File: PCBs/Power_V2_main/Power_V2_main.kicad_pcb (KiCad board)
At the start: 2 copper layers, 53 parts, among them IC2 ADS1115BQDGSRQ1, IC3 ADS1115BQDGSRQ1, J1 Conn_01x02, J11 Conn_01x04, J12 Conn_01x02, J13 Conn_01x04, J14 Conn_01x04, J18 YK4420203000G, J2 Conn_01x02, J3 Conn_01x02, J4 PCIE-164-02-F-D-TH-TR, J5 PCIE-164-02-F-D-TH-TR, J6 PCIE-164-02-F-D-TH-TR, J7 USB_C_Receptacle_USB2.0_16P, J8 PCIE-164-02-F-D-TH-TR, Q4 NTD25P03LT4G, U2 ESP32-S3, U3 USBLC6-2SC6, U4 178.6164.0001, U5 TVS3300DRV, U9 AMS1117-3.3

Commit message: finished secondary and beginning layout of main
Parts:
- moved J5 242.8 mm to (236.8, 224.2), turned to 180 degrees
- moved J1 232.2 mm to (280.0, 63.0)
- moved J3 232.2 mm to (292.3, 63.0)
- moved J2 216.7 mm to (265.5, 82.0), turned to -90 degrees
- moved J4 214.2 mm to (236.8, 199.2), turned to 180 degrees
- moved J12 198.0 mm to (265.0, 129.5), turned to 90 degrees
- moved J18 191.7 mm to (265.8, 104.8), turned to -90 degrees
- moved J6 188.7 mm to (236.8, 174.2), turned to 180 degrees
- moved J8 167.7 mm to (236.8, 149.2), turned to 180 degrees
- moved C12 116.3 mm to (9.14, 152.8)
- moved C14 116.3 mm to (-10.1, 194.6)
- moved C17 116.3 mm to (9.14, 160.4)
- moved D3 116.3 mm to (1.31, 174.0)
- moved IC3 116.3 mm to (22.8, 183.8)
- moved J7 116.3 mm to (17.2, 171.5)
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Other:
- board outline added: 100 x 200 mm

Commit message: shortened main board and secondary
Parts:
- removed the J7 at (17.2, 171.5)
- removed RESET1: PTS645SK43SMTR92LFS, IPRL_footprints:PTS645SK43SMTR92LFS
- removed S1: SK12F14G5, IPRL_footprints:SK12F14G5
- removed U4: 178.6164.0001, IPRL_footprints:178.6164.XXX1
- added J7: TYPE-C-31-M-12, iprl_footprints:TYPE-C-31-M-12, F.Cu at (142.9, 216.3)
- added J7: USB_C_Receptacle_USB2.0_16P, iprl_footprints:USB_C_16P, F.Cu at (131.9, 180.4)
- added R20: 5.1k, Resistor_SMD:R_0805_2012Metric, F.Cu at (139.1, 221.1)
- added R21: 5.1k, Resistor_SMD:R_0805_2012Metric, F.Cu at (139.1, 224.1)
- added U6: USBLC6-4SC6, Package_TO_SOT_SMD:SOT-23-6, F.Cu at (143.9, 222.1)
- BOOT1: footprint IPRL_footprints:PTS645SK43SMTR92LFS -> iprl_footprints:PTS645SK43SMTR92LFS
- D1: footprint IPRL_footprints:SODFL1608X70N -> iprl_footprints:SODFL1608X70N
- D4: footprint IPRL_footprints:DIOM8059X265N -> iprl_footprints:DIOM8059X265N
- IC2, IC3: footprint IPRL_footprints:SOP50P490X110-10N -> iprl_footprints:SOP50P490X110-10N
- J18: footprint IPRL_footprints:RHDR2W120P0X950_1X2_2050X1430X1790P -> iprl_footprints:RHDR2W120P0X950_1X2_2050X1430X1790P
- J4, J5, J6, J8: footprint IPRL_footprints:SAMTEC_PCIE-164-02-F-D-TH-TR -> iprl_footprints:SAMTEC_PCIE-164-02-F-D-TH-TR
- Q4: footprint IPRL_footprints:MJD45H11T4G -> iprl_footprints:MJD45H11T4G
- moved C14 180.9 mm to (159.9, 132.8)
- moved C9 180.9 mm to (159.9, 129.8)
- moved D4 175.6 mm to (154.4, 158.7)
- moved J1 174.3 mm to (119.9, 132.0)
- moved J3 174.3 mm to (132.1, 132.0)
- moved IC2 166.4 mm to (180.9, 127.3)
- moved IC3 166.4 mm to (180.9, 132.0)
- moved R1 166.4 mm to (179.4, 135.8)
- moved R3 166.4 mm to (179.4, 138.7)
- moved R5 166.4 mm to (179.4, 141.7)
- moved D7 165.1 mm to (156.5, 126.7)
- moved U5 161.7 mm to (159.8, 136.2)
- moved R4 159.8 mm to (161.1, 164.1)
- moved R7 159.8 mm to (161.1, 167.1)
- moved R8 159.8 mm to (161.1, 170.0)
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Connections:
- D7 pad 1: /Protection and power/14V8_PROTECTED -> /14V8_PROTECTED
- J4 pad A12: /Connector Arm/14V8_OUT -> /14V8_PROTECTED
- J4 pad A13: /Connector Arm/14V8_OUT -> /14V8_PROTECTED
- J4 pad A14: /Connector Arm/14V8_OUT -> /14V8_PROTECTED
- J4 pad A15: /Connector Arm/14V8_OUT -> /14V8_PROTECTED
- J4 pad A16: /Connector Arm/14V8_OUT -> /14V8_PROTECTED
- J4 pad A17: /Connector Arm/14V8_OUT -> /14V8_PROTECTED
- J4 pad A18: /Connector Arm/14V8_OUT -> /14V8_PROTECTED
- J4 pad A19: /Connector Arm/14V8_OUT -> /14V8_PROTECTED
- J4 pad A20: /Connector Arm/14V8_OUT -> /14V8_PROTECTED
- J4 pad A21: /Connector Arm/14V8_OUT -> /14V8_PROTECTED
- J4 pad A22: /Connector Arm/14V8_OUT -> /14V8_PROTECTED
- J4 pad A23: /Connector Arm/14V8_OUT -> /14V8_PROTECTED
- J4 pad A24: /Connector Arm/14V8_OUT -> /14V8_PROTECTED
- J4 pad A25: /Connector Arm/14V8_OUT -> /14V8_PROTECTED
- J4 pad A26: /Connector Arm/14V8_OUT -> /14V8_PROTECTED
- J4 pad A27: /Connector Arm/14V8_OUT -> /14V8_PROTECTED
- J4 pad A28: /Connector Arm/14V8_OUT -> /14V8_PROTECTED
- J4 pad A29: /Connector Arm/14V8_OUT -> /14V8_PROTECTED
- J4 pad A30: /Connector Arm/14V8_OUT -> /14V8_PROTECTED
- J4 pad A31: /Connector Arm/14V8_OUT -> /14V8_PROTECTED
- J4 pad A32: /Connector Arm/14V8_OUT -> /14V8_PROTECTED
- J4 pad A33: /Connector Arm/14V8_OUT -> /14V8_PROTECTED
- J4 pad A34: /Connector Arm/14V8_OUT -> /14V8_PROTECTED
- J4 pad A35: /Connector Arm/14V8_OUT -> /14V8_PROTECTED
- J4 pad A36: /Connector Arm/14V8_OUT -> /14V8_PROTECTED
- J4 pad A37: /Connector Arm/14V8_OUT -> /14V8_PROTECTED
- J4 pad A38: /Connector Arm/14V8_OUT -> /14V8_PROTECTED
- J4 pad A39: /Connector Arm/14V8_OUT -> /14V8_PROTECTED
- J4 pad A40: /Connector Arm/14V8_OUT -> /14V8_PROTECTED
- J4 pad A41: /Connector Arm/14V8_OUT -> /14V8_PROTECTED
- J4 pad A42: /Connector Arm/14V8_OUT -> /14V8_PROTECTED
- J4 pad A43: /Connector Arm/14V8_OUT -> /14V8_PROTECTED
- J4 pad A44: /Connector Arm/14V8_OUT -> /14V8_PROTECTED
- J4 pad A45: /Connector Arm/14V8_OUT -> /14V8_PROTECTED
- J4 pad A46: /Connector Arm/14V8_OUT -> /14V8_PROTECTED
- J4 pad A47: /Connector Arm/14V8_OUT -> /14V8_PROTECTED
- J4 pad A48: /Connector Arm/14V8_OUT -> /14V8_PROTECTED
- J4 pad A49: /Connector Arm/14V8_OUT -> /14V8_PROTECTED
- J4 pad A50: /Connector Arm/14V8_OUT -> /14V8_PROTECTED
- J4 pad A51: /Connector Arm/14V8_OUT -> /14V8_PROTECTED
- J4 pad A52: /Connector Arm/14V8_OUT -> /14V8_PROTECTED
- J4 pad A53: /Connector Arm/14V8_OUT -> /14V8_PROTECTED
- J4 pad A54: /Connector Arm/14V8_OUT -> /14V8_PROTECTED
- J4 pad A55: /Connector Arm/14V8_OUT -> /14V8_PROTECTED
- J4 pad A56: /Connector Arm/14V8_OUT -> /14V8_PROTECTED
- J4 pad A57: /Connector Arm/14V8_OUT -> /14V8_PROTECTED
- J4 pad A58: /Connector Arm/14V8_OUT -> /14V8_PROTECTED
- J4 pad A59: /Connector Arm/14V8_OUT -> /14V8_PROTECTED
- J4 pad A60: /Connector Arm/14V8_OUT -> /14V8_PROTECTED
- J4 pad A61: /Connector Arm/14V8_OUT -> /14V8_PROTECTED
- J4 pad A62: /Connector Arm/14V8_OUT -> /14V8_PROTECTED
- J4 pad A63: /Connector Arm/14V8_OUT -> /14V8_PROTECTED
- J4 pad A64: /Connector Arm/14V8_OUT -> /14V8_PROTECTED
- J4 pad A65: /Connector Arm/14V8_OUT -> /14V8_PROTECTED
- J4 pad A66: /Connector Arm/14V8_OUT -> /14V8_PROTECTED
- J4 pad A67: /Connector Arm/14V8_OUT -> /14V8_PROTECTED
- J4 pad A68: /Connector Arm/14V8_OUT -> /14V8_PROTECTED
- J4 pad A69: /Connector Arm/14V8_OUT -> /14V8_PROTECTED
- J4 pad A70: /Connector Arm/14V8_OUT -> /14V8_PROTECTED
- J4 pad A71: /Connector Arm/14V8_OUT -> /14V8_PROTECTED
- J4 pad A72: /Connector Arm/14V8_OUT -> /14V8_PROTECTED
- J4 pad A73: /Connector Arm/14V8_OUT -> /14V8_PROTECTED
- J4 pad A74: /Connector Arm/14V8_OUT -> /14V8_PROTECTED
- J4 pad A75: /Connector Arm/14V8_OUT -> /14V8_PROTECTED
- J4 pad A76: /Connector Arm/14V8_OUT -> /14V8_PROTECTED
- J4 pad A77: /Connector Arm/14V8_OUT -> /14V8_PROTECTED
- J4 pad A78: /Connector Arm/14V8_OUT -> /14V8_PROTECTED
- J4 pad A79: /Connector Arm/14V8_OUT -> /14V8_PROTECTED
- J4 pad A80: /Connector Arm/14V8_OUT -> /14V8_PROTECTED
- J4 pad A81: /Connector Arm/14V8_OUT -> /14V8_PROTECTED
- J4 pad A82: /Connector Arm/14V8_OUT -> /14V8_PROTECTED
- J5 pad A12: /Connector Comms/14V8_OUT -> /14V8_PROTECTED
- J5 pad A13: /Connector Comms/14V8_OUT -> /14V8_PROTECTED
- J5 pad A14: /Connector Comms/14V8_OUT -> /14V8_PROTECTED
- J5 pad A15: /Connector Comms/14V8_OUT -> /14V8_PROTECTED
- J5 pad A16: /Connector Comms/14V8_OUT -> /14V8_PROTECTED
- J5 pad A17: /Connector Comms/14V8_OUT -> /14V8_PROTECTED
- J5 pad A18: /Connector Comms/14V8_OUT -> /14V8_PROTECTED
- J5 pad A19: /Connector Comms/14V8_OUT -> /14V8_PROTECTED
- J5 pad A20: /Connector Comms/14V8_OUT -> /14V8_PROTECTED
- J5 pad A21: /Connector Comms/14V8_OUT -> /14V8_PROTECTED
- J5 pad A22: /Connector Comms/14V8_OUT -> /14V8_PROTECTED
- J5 pad A23: /Connector Comms/14V8_OUT -> /14V8_PROTECTED
- J5 pad A24: /Connector Comms/14V8_OUT -> /14V8_PROTECTED
- J5 pad A25: /Connector Comms/14V8_OUT -> /14V8_PROTECTED
- J5 pad A26: /Connector Comms/14V8_OUT -> /14V8_PROTECTED
- J5 pad A27: /Connector Comms/14V8_OUT -> /14V8_PROTECTED
- J5 pad A28: /Connector Comms/14V8_OUT -> /14V8_PROTECTED
- J5 pad A29: /Connector Comms/14V8_OUT -> /14V8_PROTECTED
- J5 pad A30: /Connector Comms/14V8_OUT -> /14V8_PROTECTED
- J5 pad A31: /Connector Comms/14V8_OUT -> /14V8_PROTECTED
- J5 pad A32: /Connector Comms/14V8_OUT -> /14V8_PROTECTED
- J5 pad A33: /Connector Comms/14V8_OUT -> /14V8_PROTECTED
- J5 pad A34: /Connector Comms/14V8_OUT -> /14V8_PROTECTED
- J5 pad A35: /Connector Comms/14V8_OUT -> /14V8_PROTECTED
- J5 pad A36: /Connector Comms/14V8_OUT -> /14V8_PROTECTED
- J5 pad A37: /Connector Comms/14V8_OUT -> /14V8_PROTECTED
- J5 pad A38: /Connector Comms/14V8_OUT -> /14V8_PROTECTED
- J5 pad A39: /Connector Comms/14V8_OUT -> /14V8_PROTECTED
- J5 pad A40: /Connector Comms/14V8_OUT -> /14V8_PROTECTED
- J5 pad A41: /Connector Comms/14V8_OUT -> /14V8_PROTECTED
- J5 pad A42: /Connector Comms/14V8_OUT -> /14V8_PROTECTED
- J5 pad A43: /Connector Comms/14V8_OUT -> /14V8_PROTECTED
- J5 pad A44: /Connector Comms/14V8_OUT -> /14V8_PROTECTED
- J5 pad A45: /Connector Comms/14V8_OUT -> /14V8_PROTECTED
- J5 pad A46: /Connector Comms/14V8_OUT -> /14V8_PROTECTED
- J5 pad A47: /Connector Comms/14V8_OUT -> /14V8_PROTECTED
- J5 pad A48: /Connector Comms/14V8_OUT -> /14V8_PROTECTED
- J5 pad A49: /Connector Comms/14V8_OUT -> /14V8_PROTECTED
- J5 pad A50: /Connector Comms/14V8_OUT -> /14V8_PROTECTED
- J5 pad A51: /Connector Comms/14V8_OUT -> /14V8_PROTECTED
- J5 pad A52: /Connector Comms/14V8_OUT -> /14V8_PROTECTED
- J5 pad A53: /Connector Comms/14V8_OUT -> /14V8_PROTECTED
- J5 pad A54: /Connector Comms/14V8_OUT -> /14V8_PROTECTED
- J5 pad A55: /Connector Comms/14V8_OUT -> /14V8_PROTECTED
- J5 pad A56: /Connector Comms/14V8_OUT -> /14V8_PROTECTED
- J5 pad A57: /Connector Comms/14V8_OUT -> /14V8_PROTECTED
- J5 pad A58: /Connector Comms/14V8_OUT -> /14V8_PROTECTED
- J5 pad A59: /Connector Comms/14V8_OUT -> /14V8_PROTECTED
- J5 pad A60: /Connector Comms/14V8_OUT -> /14V8_PROTECTED
- J5 pad A61: /Connector Comms/14V8_OUT -> /14V8_PROTECTED
- J5 pad A62: /Connector Comms/14V8_OUT -> /14V8_PROTECTED
- J5 pad A63: /Connector Comms/14V8_OUT -> /14V8_PROTECTED
- J5 pad A64: /Connector Comms/14V8_OUT -> /14V8_PROTECTED
- J5 pad A65: /Connector Comms/14V8_OUT -> /14V8_PROTECTED
- J5 pad A66: /Connector Comms/14V8_OUT -> /14V8_PROTECTED
- J5 pad A67: /Connector Comms/14V8_OUT -> /14V8_PROTECTED
- J5 pad A68: /Connector Comms/14V8_OUT -> /14V8_PROTECTED
- J5 pad A69: /Connector Comms/14V8_OUT -> /14V8_PROTECTED
- J5 pad A70: /Connector Comms/14V8_OUT -> /14V8_PROTECTED
- J5 pad A71: /Connector Comms/14V8_OUT -> /14V8_PROTECTED
- J5 pad A72: /Connector Comms/14V8_OUT -> /14V8_PROTECTED
- J5 pad A73: /Connector Comms/14V8_OUT -> /14V8_PROTECTED
- J5 pad A74: /Connector Comms/14V8_OUT -> /14V8_PROTECTED
- J5 pad A75: /Connector Comms/14V8_OUT -> /14V8_PROTECTED
- J5 pad A76: /Connector Comms/14V8_OUT -> /14V8_PROTECTED
- J5 pad A77: /Connector Comms/14V8_OUT -> /14V8_PROTECTED
- J5 pad A78: /Connector Comms/14V8_OUT -> /14V8_PROTECTED
- J5 pad A79: /Connector Comms/14V8_OUT -> /14V8_PROTECTED
- J5 pad A80: /Connector Comms/14V8_OUT -> /14V8_PROTECTED
- J5 pad A81: /Connector Comms/14V8_OUT -> /14V8_PROTECTED
- J5 pad A82: /Connector Comms/14V8_OUT -> /14V8_PROTECTED
- J6 pad A12: /Connector Drive/14V8_OUT -> /14V8_PROTECTED
- J6 pad A13: /Connector Drive/14V8_OUT -> /14V8_PROTECTED
- J6 pad A14: /Connector Drive/14V8_OUT -> /14V8_PROTECTED
- J6 pad A15: /Connector Drive/14V8_OUT -> /14V8_PROTECTED
- J6 pad A16: /Connector Drive/14V8_OUT -> /14V8_PROTECTED
- J6 pad A17: /Connector Drive/14V8_OUT -> /14V8_PROTECTED
- J6 pad A18: /Connector Drive/14V8_OUT -> /14V8_PROTECTED
- J6 pad A19: /Connector Drive/14V8_OUT -> /14V8_PROTECTED
- J6 pad A20: /Connector Drive/14V8_OUT -> /14V8_PROTECTED
- J6 pad A21: /Connector Drive/14V8_OUT -> /14V8_PROTECTED
- J6 pad A22: /Connector Drive/14V8_OUT -> /14V8_PROTECTED
- J6 pad A23: /Connector Drive/14V8_OUT -> /14V8_PROTECTED
- J6 pad A24: /Connector Drive/14V8_OUT -> /14V8_PROTECTED
- J6 pad A25: /Connector Drive/14V8_OUT -> /14V8_PROTECTED
- J6 pad A26: /Connector Drive/14V8_OUT -> /14V8_PROTECTED
- J6 pad A27: /Connector Drive/14V8_OUT -> /14V8_PROTECTED
- J6 pad A28: /Connector Drive/14V8_OUT -> /14V8_PROTECTED
- J6 pad A29: /Connector Drive/14V8_OUT -> /14V8_PROTECTED
- J6 pad A30: /Connector Drive/14V8_OUT -> /14V8_PROTECTED
- J6 pad A31: /Connector Drive/14V8_OUT -> /14V8_PROTECTED
- J6 pad A32: /Connector Drive/14V8_OUT -> /14V8_PROTECTED
- J6 pad A33: /Connector Drive/14V8_OUT -> /14V8_PROTECTED
- J6 pad A34: /Connector Drive/14V8_OUT -> /14V8_PROTECTED
- J6 pad A35: /Connector Drive/14V8_OUT -> /14V8_PROTECTED
- J6 pad A36: /Connector Drive/14V8_OUT -> /14V8_PROTECTED
- J6 pad A37: /Connector Drive/14V8_OUT -> /14V8_PROTECTED
- J6 pad A38: /Connector Drive/14V8_OUT -> /14V8_PROTECTED
- J6 pad A39: /Connector Drive/14V8_OUT -> /14V8_PROTECTED
- J6 pad A40: /Connector Drive/14V8_OUT -> /14V8_PROTECTED
- J6 pad A41: /Connector Drive/14V8_OUT -> /14V8_PROTECTED
- J6 pad A42: /Connector Drive/14V8_OUT -> /14V8_PROTECTED
- J6 pad A43: /Connector Drive/14V8_OUT -> /14V8_PROTECTED
- J6 pad A44: /Connector Drive/14V8_OUT -> /14V8_PROTECTED
- J6 pad A45: /Connector Drive/14V8_OUT -> /14V8_PROTECTED
- J6 pad A46: /Connector Drive/14V8_OUT -> /14V8_PROTECTED
- J6 pad A47: /Connector Drive/14V8_OUT -> /14V8_PROTECTED
- J6 pad A48: /Connector Drive/14V8_OUT -> /14V8_PROTECTED
- J6 pad A49: /Connector Drive/14V8_OUT -> /14V8_PROTECTED
- J6 pad A50: /Connector Drive/14V8_OUT -> /14V8_PROTECTED
- J6 pad A51: /Connector Drive/14V8_OUT -> /14V8_PROTECTED
- J6 pad A52: /Connector Drive/14V8_OUT -> /14V8_PROTECTED
- J6 pad A53: /Connector Drive/14V8_OUT -> /14V8_PROTECTED
- J6 pad A54: /Connector Drive/14V8_OUT -> /14V8_PROTECTED
- J6 pad A55: /Connector Drive/14V8_OUT -> /14V8_PROTECTED
- J6 pad A56: /Connector Drive/14V8_OUT -> /14V8_PROTECTED
- J6 pad A57: /Connector Drive/14V8_OUT -> /14V8_PROTECTED
- J6 pad A58: /Connector Drive/14V8_OUT -> /14V8_PROTECTED
- J6 pad A59: /Connector Drive/14V8_OUT -> /14V8_PROTECTED
- J6 pad A60: /Connector Drive/14V8_OUT -> /14V8_PROTECTED
- J6 pad A61: /Connector Drive/14V8_OUT -> /14V8_PROTECTED
- J6 pad A62: /Connector Drive/14V8_OUT -> /14V8_PROTECTED
- J6 pad A63: /Connector Drive/14V8_OUT -> /14V8_PROTECTED
- J6 pad A64: /Connector Drive/14V8_OUT -> /14V8_PROTECTED
- J6 pad A65: /Connector Drive/14V8_OUT -> /14V8_PROTECTED
- J6 pad A66: /Connector Drive/14V8_OUT -> /14V8_PROTECTED
- J6 pad A67: /Connector Drive/14V8_OUT -> /14V8_PROTECTED
- J6 pad A68: /Connector Drive/14V8_OUT -> /14V8_PROTECTED
- J6 pad A69: /Connector Drive/14V8_OUT -> /14V8_PROTECTED
- J6 pad A70: /Connector Drive/14V8_OUT -> /14V8_PROTECTED
- J6 pad A71: /Connector Drive/14V8_OUT -> /14V8_PROTECTED
- J6 pad A72: /Connector Drive/14V8_OUT -> /14V8_PROTECTED
- J6 pad A73: /Connector Drive/14V8_OUT -> /14V8_PROTECTED
- J6 pad A74: /Connector Drive/14V8_OUT -> /14V8_PROTECTED
- J6 pad A75: /Connector Drive/14V8_OUT -> /14V8_PROTECTED
- J6 pad A76: /Connector Drive/14V8_OUT -> /14V8_PROTECTED
- J6 pad A77: /Connector Drive/14V8_OUT -> /14V8_PROTECTED
- J6 pad A78: /Connector Drive/14V8_OUT -> /14V8_PROTECTED
- J6 pad A79: /Connector Drive/14V8_OUT -> /14V8_PROTECTED
- J6 pad A80: /Connector Drive/14V8_OUT -> /14V8_PROTECTED
- J6 pad A81: /Connector Drive/14V8_OUT -> /14V8_PROTECTED
- J6 pad A82: /Connector Drive/14V8_OUT -> /14V8_PROTECTED
- J8 pad A12: /Connector Drill/14V8_OUT -> /14V8_PROTECTED
- J8 pad A13: /Connector Drill/14V8_OUT -> /14V8_PROTECTED
- J8 pad A14: /Connector Drill/14V8_OUT -> /14V8_PROTECTED
- J8 pad A15: /Connector Drill/14V8_OUT -> /14V8_PROTECTED
- J8 pad A16: /Connector Drill/14V8_OUT -> /14V8_PROTECTED
- J8 pad A17: /Connector Drill/14V8_OUT -> /14V8_PROTECTED
- J8 pad A18: /Connector Drill/14V8_OUT -> /14V8_PROTECTED
- J8 pad A19: /Connector Drill/14V8_OUT -> /14V8_PROTECTED
- J8 pad A20: /Connector Drill/14V8_OUT -> /14V8_PROTECTED
- J8 pad A21: /Connector Drill/14V8_OUT -> /14V8_PROTECTED
- J8 pad A22: /Connector Drill/14V8_OUT -> /14V8_PROTECTED
- J8 pad A23: /Connector Drill/14V8_OUT -> /14V8_PROTECTED
- J8 pad A24: /Connector Drill/14V8_OUT -> /14V8_PROTECTED
- J8 pad A25: /Connector Drill/14V8_OUT -> /14V8_PROTECTED
- J8 pad A26: /Connector Drill/14V8_OUT -> /14V8_PROTECTED
- J8 pad A27: /Connector Drill/14V8_OUT -> /14V8_PROTECTED
- J8 pad A28: /Connector Drill/14V8_OUT -> /14V8_PROTECTED
- J8 pad A29: /Connector Drill/14V8_OUT -> /14V8_PROTECTED
- J8 pad A30: /Connector Drill/14V8_OUT -> /14V8_PROTECTED
- J8 pad A31: /Connector Drill/14V8_OUT -> /14V8_PROTECTED
- J8 pad A32: /Connector Drill/14V8_OUT -> /14V8_PROTECTED
- J8 pad A33: /Connector Drill/14V8_OUT -> /14V8_PROTECTED
- J8 pad A34: /Connector Drill/14V8_OUT -> /14V8_PROTECTED
- J8 pad A35: /Connector Drill/14V8_OUT -> /14V8_PROTECTED
- J8 pad A36: /Connector Drill/14V8_OUT -> /14V8_PROTECTED
- J8 pad A37: /Connector Drill/14V8_OUT -> /14V8_PROTECTED
- J8 pad A38: /Connector Drill/14V8_OUT -> /14V8_PROTECTED
- J8 pad A39: /Connector Drill/14V8_OUT -> /14V8_PROTECTED
- J8 pad A40: /Connector Drill/14V8_OUT -> /14V8_PROTECTED
- J8 pad A41: /Connector Drill/14V8_OUT -> /14V8_PROTECTED
- J8 pad A42: /Connector Drill/14V8_OUT -> /14V8_PROTECTED
- J8 pad A43: /Connector Drill/14V8_OUT -> /14V8_PROTECTED
- J8 pad A44: /Connector Drill/14V8_OUT -> /14V8_PROTECTED
- J8 pad A45: /Connector Drill/14V8_OUT -> /14V8_PROTECTED
- J8 pad A46: /Connector Drill/14V8_OUT -> /14V8_PROTECTED
- J8 pad A47: /Connector Drill/14V8_OUT -> /14V8_PROTECTED
- J8 pad A48: /Connector Drill/14V8_OUT -> /14V8_PROTECTED
- J8 pad A49: /Connector Drill/14V8_OUT -> /14V8_PROTECTED
- J8 pad A50: /Connector Drill/14V8_OUT -> /14V8_PROTECTED
- J8 pad A51: /Connector Drill/14V8_OUT -> /14V8_PROTECTED
- J8 pad A52: /Connector Drill/14V8_OUT -> /14V8_PROTECTED
- J8 pad A53: /Connector Drill/14V8_OUT -> /14V8_PROTECTED
- J8 pad A54: /Connector Drill/14V8_OUT -> /14V8_PROTECTED
- J8 pad A55: /Connector Drill/14V8_OUT -> /14V8_PROTECTED
- J8 pad A56: /Connector Drill/14V8_OUT -> /14V8_PROTECTED
- J8 pad A57: /Connector Drill/14V8_OUT -> /14V8_PROTECTED
- J8 pad A58: /Connector Drill/14V8_OUT -> /14V8_PROTECTED
- J8 pad A59: /Connector Drill/14V8_OUT -> /14V8_PROTECTED
- J8 pad A60: /Connector Drill/14V8_OUT -> /14V8_PROTECTED
- J8 pad A61: /Connector Drill/14V8_OUT -> /14V8_PROTECTED
- J8 pad A62: /Connector Drill/14V8_OUT -> /14V8_PROTECTED
- J8 pad A63: /Connector Drill/14V8_OUT -> /14V8_PROTECTED
- J8 pad A64: /Connector Drill/14V8_OUT -> /14V8_PROTECTED
- J8 pad A65: /Connector Drill/14V8_OUT -> /14V8_PROTECTED
- J8 pad A66: /Connector Drill/14V8_OUT -> /14V8_PROTECTED
- J8 pad A67: /Connector Drill/14V8_OUT -> /14V8_PROTECTED
- J8 pad A68: /Connector Drill/14V8_OUT -> /14V8_PROTECTED
- J8 pad A69: /Connector Drill/14V8_OUT -> /14V8_PROTECTED
- J8 pad A70: /Connector Drill/14V8_OUT -> /14V8_PROTECTED
- J8 pad A71: /Connector Drill/14V8_OUT -> /14V8_PROTECTED
- J8 pad A72: /Connector Drill/14V8_OUT -> /14V8_PROTECTED
- J8 pad A73: /Connector Drill/14V8_OUT -> /14V8_PROTECTED
- J8 pad A74: /Connector Drill/14V8_OUT -> /14V8_PROTECTED
- J8 pad A75: /Connector Drill/14V8_OUT -> /14V8_PROTECTED
- J8 pad A76: /Connector Drill/14V8_OUT -> /14V8_PROTECTED
- J8 pad A77: /Connector Drill/14V8_OUT -> /14V8_PROTECTED
- J8 pad A78: /Connector Drill/14V8_OUT -> /14V8_PROTECTED
- J8 pad A79: /Connector Drill/14V8_OUT -> /14V8_PROTECTED
- J8 pad A80: /Connector Drill/14V8_OUT -> /14V8_PROTECTED
- J8 pad A81: /Connector Drill/14V8_OUT -> /14V8_PROTECTED
- J8 pad A82: /Connector Drill/14V8_OUT -> /14V8_PROTECTED
- Q4 pad 3: /Protection and power/14V8_PROTECTED -> /14V8_PROTECTED
- R1 pad 1: /Protection and power/14V8_PROTECTED -> /14V8_PROTECTED
- U5 pad 4: /Protection and power/14V8_PROTECTED -> /14V8_PROTECTED
- U5 pad 5: /Protection and power/14V8_PROTECTED -> /14V8_PROTECTED
- U5 pad 6: /Protection and power/14V8_PROTECTED -> /14V8_PROTECTED
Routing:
- added copper zone on F.Cu, net /14V8_PROTECTED
- added copper zone on B.Cu, net GND
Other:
- board size 100 x 200 mm -> 100 x 100 mm

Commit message: corrected power to main
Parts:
- removed D6: MBRA340T3G, Diode_SMD:D_SMA
- removed the J7 at (131.9, 180.4)
- removed R10, R9: 5k, Resistor_SMD:R_0805_2012Metric
- removed U3: USBLC6-2SC6, Package_TO_SOT_SMD:SOT-23-6
- J11, J13, J14: footprint Connector_JST:JST_PH_S4B-PH-K_1x04_P2.00mm_Horizontal -> Connector_JST:JST_GH_SM04B-GHS-TB_1x04-1MP_P1.25mm_Horizontal
- moved D4 124.4 mm to (278.8, 161.8)
- moved Q4 124.4 mm to (268.6, 166.1)
- moved R4 124.4 mm to (285.5, 167.1)
- moved R7 124.4 mm to (285.5, 170.1)
- moved R8 124.4 mm to (285.5, 173.0)
- moved U9 124.4 mm to (278.3, 169.8)
- moved U2 94.5 mm to (228.6, 153.4)
- moved R21 93.9 mm to (185.3, 142.3), turned to -90 degrees
- moved R20 92.9 mm to (188.2, 142.3), turned to -90 degrees
- moved U6 86.7 mm to (187.3, 147.1), turned to -90 degrees
- moved J7 86.2 mm to (193.1, 146.1), turned to -90 degrees
- moved J11 79.0 mm to (246.7, 136.3), turned to 180 degrees
- moved J13 67.7 mm to (236.0, 136.3), turned to 180 degrees
- moved J14 58.4 mm to (225.7, 136.3), turned to 180 degrees

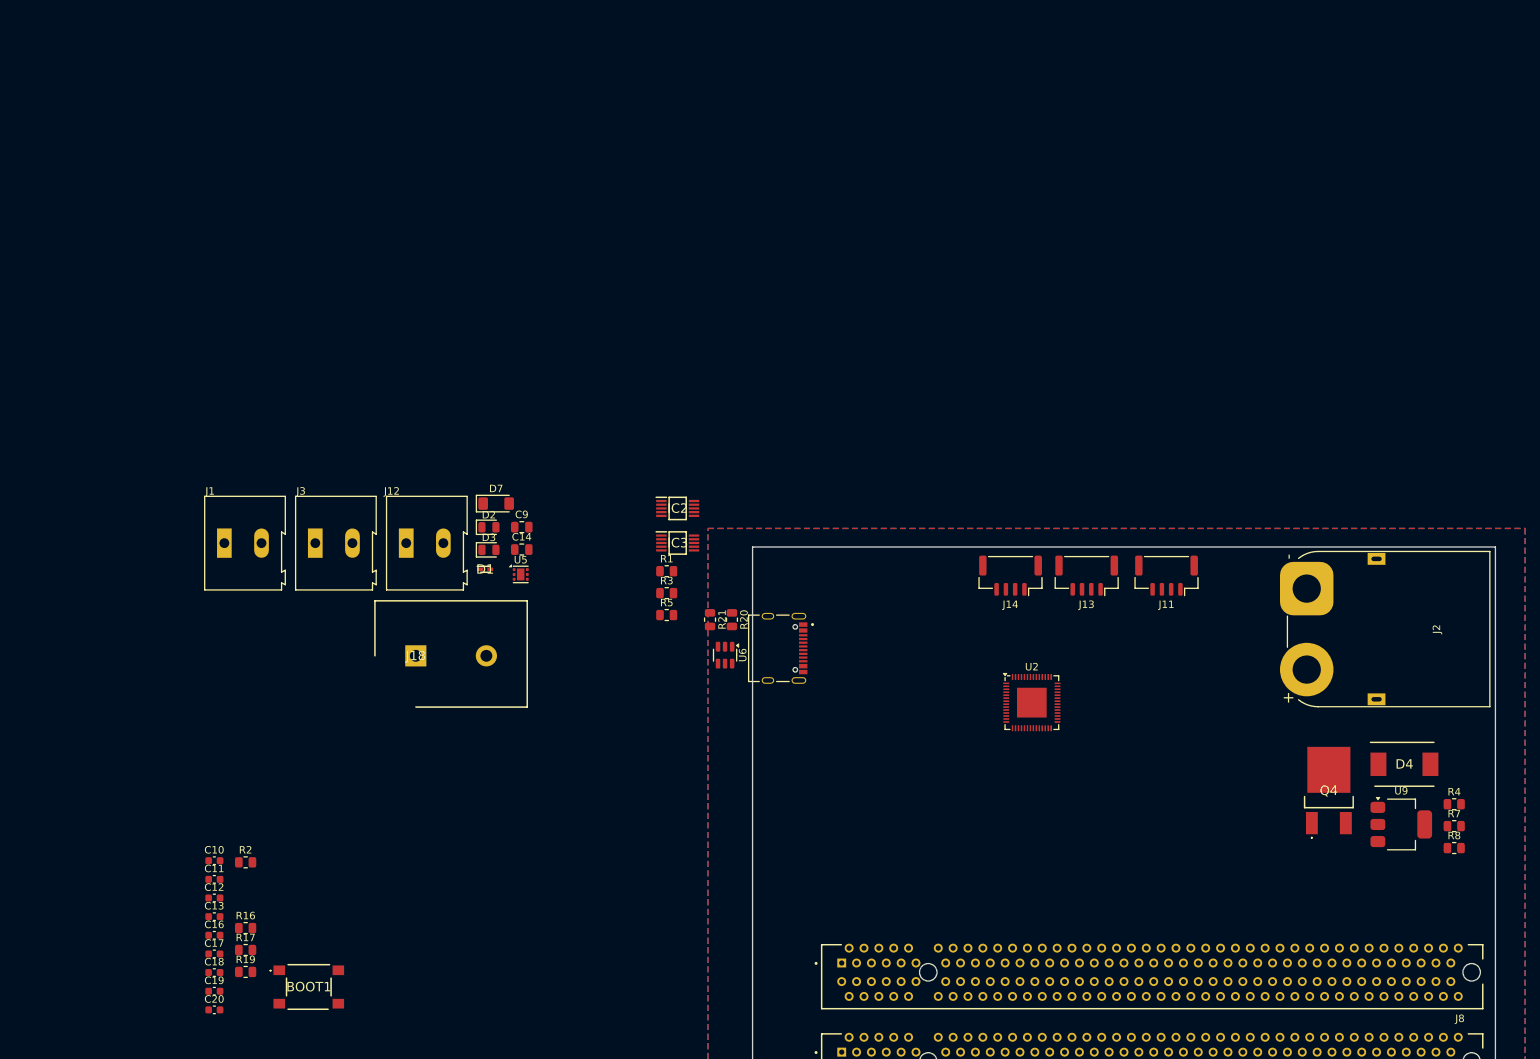
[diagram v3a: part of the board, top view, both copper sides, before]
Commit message: main schematic for power board main
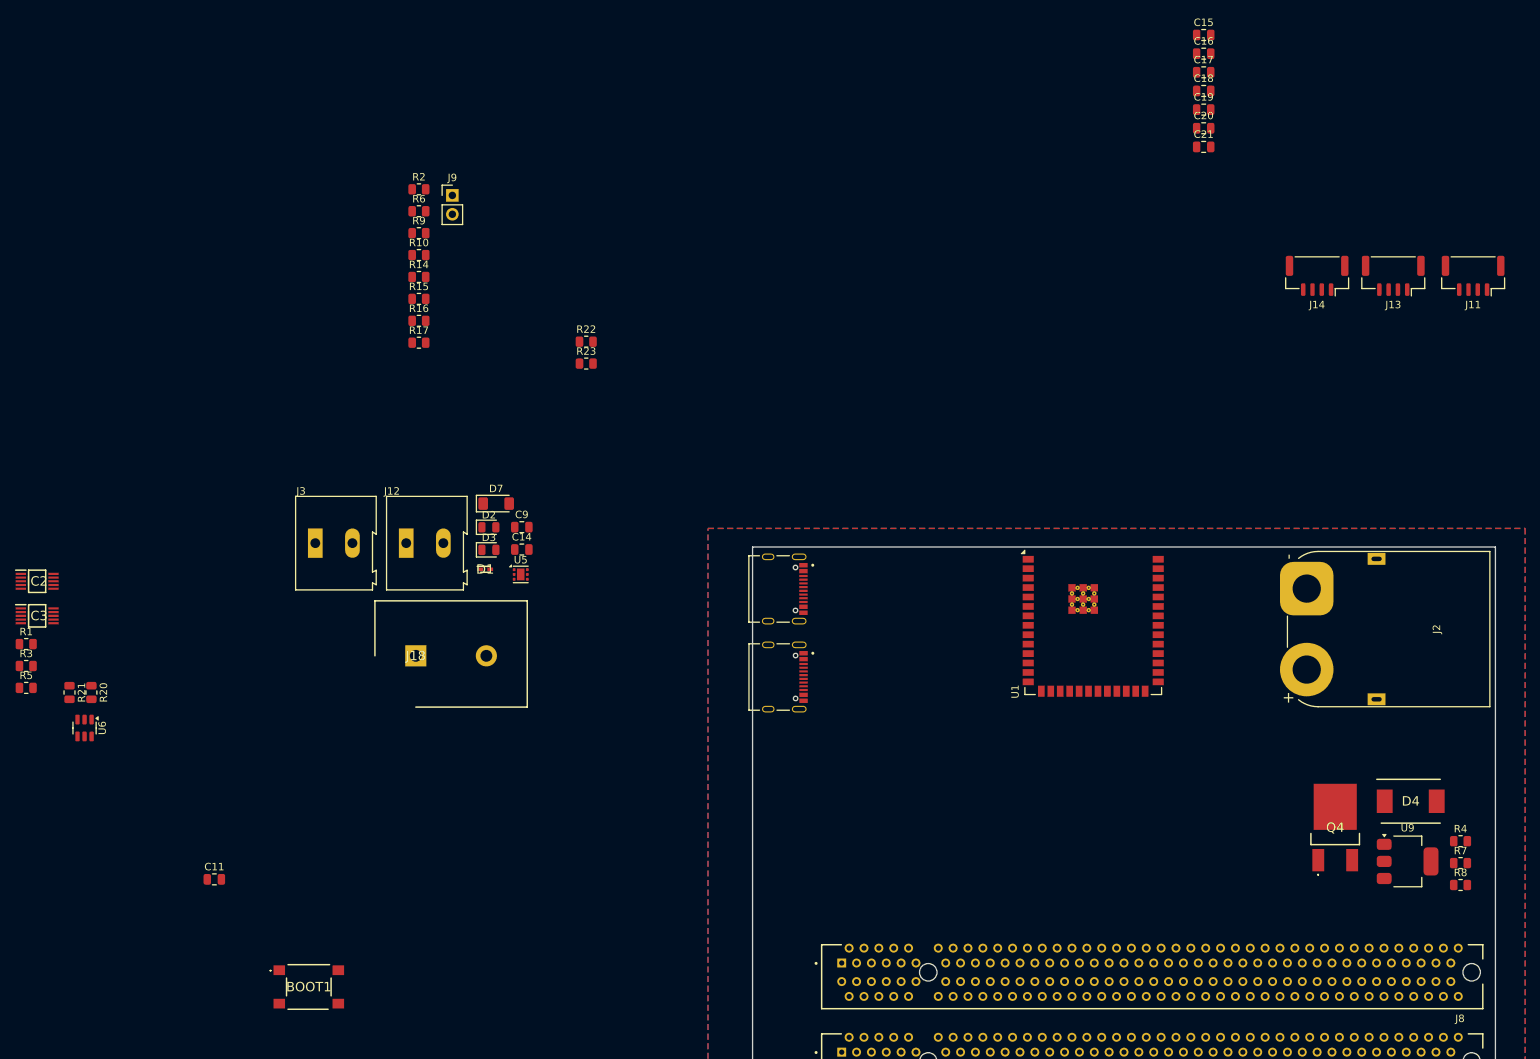
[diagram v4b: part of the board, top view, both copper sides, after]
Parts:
- removed C10: 1u, Capacitor_SMD:C_0603_1608Metric
- removed C12, C13: 0.1u, Capacitor_SMD:C_0603_1608Metric
- removed J1: Conn_01x02, TerminalBlock:TerminalBlock_Altech_AK300-2_P5.00mm
- removed R19: 56, Resistor_SMD:R_0805_2012Metric
- removed U2: ESP32-S3, Package_DFN_QFN:QFN-56-1EP_7x7mm_P0.4mm_EP4x4mm
- added C15: 0.1u, Capacitor_SMD:C_0805_2012Metric, F.Cu at (251.7, 63.6)
- added C21: 1u, Capacitor_SMD:C_0805_2012Metric, F.Cu at (251.7, 78.6)
- added J10: TYPE-C-31-M-12, iprl_footprints:TYPE-C-31-M-12, F.Cu at (193.1, 138.2)
- added J9: Conn_01x02, Connector_PinHeader_2.54mm:PinHeader_1x02_P2.54mm_Vertical, F.Cu at (150.6, 85.2)
- added R10: 10k, Resistor_SMD:R_0805_2012Metric, F.Cu at (146.1, 93.2)
- added R14: 10k, Resistor_SMD:R_0805_2012Metric, F.Cu at (146.1, 96.2)
- added R15: 10k, Resistor_SMD:R_0805_2012Metric, F.Cu at (146.1, 99.1)
- added R22: 5k, Resistor_SMD:R_0805_2012Metric, F.Cu at (168.6, 104.9)
- added R23: 5k, Resistor_SMD:R_0805_2012Metric, F.Cu at (168.6, 107.8)
- added R6: 0R, Resistor_SMD:R_0805_2012Metric, F.Cu at (146.1, 87.3)
- added R9: 10k, Resistor_SMD:R_0805_2012Metric, F.Cu at (146.1, 90.2)
- added U1: ESP32-S3-WROOM-2, RF_Module:ESP32-S3-WROOM-2, F.Cu at (236.9, 139.4)
- C11: footprint Capacitor_SMD:C_0603_1608Metric -> Capacitor_SMD:C_0805_2012Metric
- C16: value 10p -> 1u; footprint Capacitor_SMD:C_0603_1608Metric -> Capacitor_SMD:C_0805_2012Metric
- C17: value 10p -> 100n; footprint Capacitor_SMD:C_0603_1608Metric -> Capacitor_SMD:C_0805_2012Metric
- C18, C19, C20: value 0.1u -> 1u; footprint Capacitor_SMD:C_0603_1608Metric -> Capacitor_SMD:C_0805_2012Metric
- R17: value 56 -> 10k
- moved C16 178.4 mm to (251.7, 66.1)
- moved C17 178.4 mm to (251.7, 68.6)
- moved C19 178.4 mm to (251.7, 73.6)
- moved C20 178.4 mm to (251.7, 76.1)
- moved C18 178.4 mm to (251.7, 71.1)
- moved R2 93.6 mm to (146.1, 84.3)
- moved R21 86.8 mm to (99.0, 152.1)
- moved U6 86.8 mm to (101.1, 156.9)
- moved IC2 86.8 mm to (94.7, 137.1)
- moved IC3 86.8 mm to (94.7, 141.8)
- moved R1 86.8 mm to (93.2, 145.6)
- moved R20 86.8 mm to (102.0, 152.1)
- moved R3 86.8 mm to (93.2, 148.5)
- moved R5 86.8 mm to (93.2, 151.5)
- moved R16 85.0 mm to (146.1, 102.0)
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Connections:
- BOOT1 pad 1: GND -> Net-(BOOT1-NO_1)
- BOOT1 pad 2: GND -> Net-(BOOT1-NO_1)
- BOOT1 pad 3: Net-(BOOT1-COM_1) -> GND
- BOOT1 pad 4: Net-(BOOT1-COM_1) -> GND
- C11 pad 1: GND -> +3.3V
- C11 pad 2: +3.3V -> GND
- C16 pad 1: GND -> /Control/EN
- C16 pad 2: /Control/XTAL_N -> GND
- C17 pad 1: /Control/XTAL_P -> GND
- C17 pad 2: GND -> Net-(BOOT1-NO_1)
- C18 pad 1: GND -> /ARM_PLUGGED
- C18 pad 2: +3.3V -> GND
- C19 pad 1: GND -> /DRIVE_PLUGGED
- C19 pad 2: +3.3V -> GND
- C20 pad 1: GND -> /COMMS_PLUGGED
- C20 pad 2: +3.3V -> GND
- J4 pad A1: /Connector Arm/OUT_READ -> /ARM_PLUGGED
- J5 pad A1: /Connector Comms/OUT_READ -> /COMMS_PLUGGED
- J6 pad A1: /Connector Drive/OUT_READ -> /DRIVE_PLUGGED
- J8 pad A1: /Connector Drill/OUT_READ -> /DRILL_PLUGGED
- R16 pad 1: Net-(BOOT1-COM_1) -> +3.3V
- R16 pad 2: +3.3V -> /COMMS_PLUGGED
- R17 pad 1: Net-(RESET1-NO_1) -> +3.3V
- R17 pad 2: Net-(LED1-A_GREEN) -> /DRILL_PLUGGED
- R2 pad 1: Net-(RESET1-NO_1) -> +3.3V
- R2 pad 2: +3.3V -> /Control/EN

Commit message: a 5 hour binge of PCB layout on the main
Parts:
- removed C18, C19, C20, C21: 1u, Capacitor_SMD:C_0805_2012Metric
- removed D7: BZV55B10, Diode_SMD:D_MiniMELF
- removed J14: Conn_01x04, Connector_JST:JST_GH_SM04B-GHS-TB_1x04-1MP_P1.25mm_Horizontal
- removed Q4: NTD25P03LT4G, iprl_footprints:MJD45H11T4G
- removed R14, R15, R16, R17: 10k, Resistor_SMD:R_0805_2012Metric
- removed R4: 1k, Resistor_SMD:R_0805_2012Metric
- removed R6: 0R, Resistor_SMD:R_0805_2012Metric
- added D6: MBRA340T3G, Diode_SMD:D_SMA, F.Cu at (203.1, 156.9)
- added H1: MountingHole, MountingHole:MountingHole_2.5mm, F.Cu at (287.5, 136.0)
- added H2: MountingHole, MountingHole:MountingHole_2.5mm, F.Cu at (194.5, 229.0)
- added H3: MountingHole, MountingHole:MountingHole_2.5mm, F.Cu at (194.5, 136.0)
- added R11: 63, Resistor_SMD:R_0805_2012Metric, F.Cu at (249.7, 142.0)
- added S1: SK12F14G5, iprl_footprints:SK12F14G5, F.Cu at (259.0, 137.0)
- added U4: 178.6164.0001, iprl_footprints:178.6164.XXX1, F.Cu at (265.6, 148.5)
- moved R3 152.3 mm to (245.5, 152.0), turned to 90 degrees
- moved R1 150.4 mm to (243.5, 152.0), turned to -90 degrees
- moved IC2 146.6 mm to (240.7, 150.5), turned to 90 degrees
- moved IC3 142.3 mm to (236.7, 150.5), turned to 90 degrees
- moved R5 142.1 mm to (235.3, 154.6), turned to 180 degrees
- moved J18 138.2 mm to (283.7, 154.8), turned to 90 degrees
- moved J12 129.0 mm to (273.2, 139.5), turned to 180 degrees
- moved J11 117.7 mm to (194.7, 167.7), turned to -90 degrees
- moved J13 116.0 mm to (194.7, 177.5), turned to -90 degrees
- moved J3 111.7 mm to (243.2, 144.0), turned to 180 degrees
- moved U6 106.2 mm to (207.2, 159.2), turned to 0 degrees
- moved J9 102.1 mm to (219.0, 161.0), turned to 90 degrees
- moved R21 101.3 mm to (200.1, 159.5), turned to 90 degrees
- moved R10 101.2 mm to (233.4, 144.4), turned to 90 degrees
- moved R9 101.0 mm to (233.4, 140.9), turned to -90 degrees
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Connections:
- BOOT1 pad 1: Net-(BOOT1-NO_1) -> /Control/EN
- BOOT1 pad 2: Net-(BOOT1-NO_1) -> /Control/EN
- C17 pad 2: Net-(BOOT1-NO_1) -> /Control/EN
- D4 pad 1: /Protection and power/PROTEC_IN -> /14V8_PROTECTED
- IC2 pad 1: Net-(IC2-ADDR) -> +3.3V
- IC2 pad 4: unconnected-(IC2-AIN0-Pad4) -> /Connector Drill/OUT_READ
- IC2 pad 5: Net-(IC2-AIN1) -> /Connector Drive/OUT_READ
- IC2 pad 6: /Connector Comms/OUT_READ -> Net-(IC2-AIN2)
- IC2 pad 7: /Connector Drill/OUT_READ -> unconnected-(IC2-AIN3-Pad7)
- IC3 pad 1: +3.3V -> Net-(IC3-ADDR)
- IC3 pad 4: /Connector Arm/OUT_READ -> /Connector Comms/OUT_READ
- IC3 pad 5: /Connector Drive/OUT_READ -> /Connector Arm/OUT_READ
- J12 pad 1: /Protection and power/EMERG_OUT -> GND
- J12 pad 2: GND -> Net-(J12-Pin_2)
- J3 pad 1: /Protection and power/EMERG_OUT -> Net-(J3-Pin_1)
- J3 pad 2: Net-(J3-Pin_2) -> /Protection and power/EMERG_OUT
- J4 pad A1: /ARM_PLUGGED -> /Connector Arm/OUT_READ
- J5 pad A1: /COMMS_PLUGGED -> /Connector Comms/OUT_READ
- J6 pad A1: /DRIVE_PLUGGED -> /Connector Drive/OUT_READ
- J8 pad A1: /DRILL_PLUGGED -> /Connector Drill/OUT_READ
- R1 pad 2: Net-(IC2-AIN1) -> Net-(IC2-AIN2)
- R3 pad 1: Net-(IC2-AIN1) -> Net-(IC2-AIN2)
- R5 pad 2: Net-(IC2-ADDR) -> Net-(IC3-ADDR)
- U1 pad 15: /ARM_PLUGGED -> unconnected-(U1-IO3-Pad15)
- U1 pad 4: /DRIVE_PLUGGED -> unconnected-(U1-IO4-Pad4)
- U1 pad 5: /COMMS_PLUGGED -> unconnected-(U1-IO5-Pad5)
- U1 pad 6: /DRILL_PLUGGED -> unconnected-(U1-IO6-Pad6)
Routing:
- net /Connector Comms/OUT_READ: track 0.00 -> 121.5 mm
- net /Connector Arm/OUT_READ: track 0.00 -> 108.9 mm
- net GND: track 0.00 -> 104.3 mm, vias 0 -> 11
- net /Connector Drill/OUT_READ: track 0.00 -> 98.1 mm
- net /Control/SCL: track 0.00 -> 81.6 mm, vias 0 -> 2
- net /Control/SDA: track 0.00 -> 80.5 mm, vias 0 -> 2
- net +3.3V: track 0.00 -> 77.7 mm, vias 0 -> 7
- net /Connector Drive/OUT_READ: track 0.00 -> 76.2 mm
- net /Protection and power/14V8_IN: track 0.00 -> 55.8 mm
- net /Control/EN: track 0.00 -> 38.1 mm, vias 0 -> 2
- net +5V: track 0.00 -> 35.7 mm, vias 0 -> 2
- net /Control/USB_OUT_N: track 0.00 -> 31.1 mm, vias 0 -> 2
- net /Control/USB_OUT_P: track 0.00 -> 24.4 mm
- net /Control/VBUS: track 0.00 -> 19.7 mm
- net Net-(J12-Pin_2): track 0.00 -> 18.0 mm
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- added copper zone on F.Cu, net +3.3V
- added copper zone on F.Cu, net /Protection and power/14V8_IN
- added copper zone on F.Cu, net /Protection and power/RELAY_OUT
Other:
- outline, holes or cut-outs redrawn
